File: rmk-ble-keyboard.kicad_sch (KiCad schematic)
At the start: 1 part

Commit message: add matrix
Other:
- added sheet matrix (matrix.kicad_sch)
- title: (none) -> rmk-ble-keyboard
- moved on the sheet: U1
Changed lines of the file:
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@@
 	(generator_version "8.0")
 	(paper "A4")
+	(title_block
+		(title "rmk-ble-keyboard")
+		(date "2024-05-03")
+		(rev "0")
+	)
 	(symbol
 		(lib_id "E73_2G4M08S1C:E73-2G4M08S1C")
-		(at 147.32 88.9 0)
+		(at 60.96 49.53 0)
 		(unit 1)
 		(exclude_from_sim no)
@@
 		(fields_autoplaced yes)
 		(property "Reference" "U1"
-			(at 146.685 59.69 0)
+			(at 60.325 20.32 0)
 			(effects
 				(font
@@
 		)
 		(property "Value" "~"
-			(at 146.685 62.23 0)
+			(at 60.325 22.86 0)
 			(effects
 				(font
@@
 		)
 		(property "Footprint" "E73_2G4M08S1C:E73(2G4M08S1C)"
-			(at 147.32 88.9 0)
+			(at 60.96 49.53 0)
 			(effects
 				(font
@@
 		)
 		(property "Datasheet" ""
-			(at 147.32 88.9 0)
+			(at 60.96 49.53 0)
 			(effects
 				(font
@@
 		)
 		(property "Description" ""
-			(at 147.32 88.9 0)
+			(at 60.96 49.53 0)
 			(effects
 				(font
@@
 				)
 			)
+		)
+	)
+	(sheet
+		(at 246.38 20.32)
+		(size 33.02 138.43)
+		(fields_autoplaced yes)
+		(stroke
+			(width 0.1524)
+			(type solid)
+		)
+		(fill
+			(color 0 0 0 0.0000)
+		)
+		(property "Sheetname" "matrix"
+			(at 246.38 19.6084 0)
+			(effects
+				(font
+					(size 1.27 1.27)
+				)
+				(justify left bottom)
+			)
+		)
+		(property "Sheetfile" "matrix.kicad_sch"
+			(at 246.38 159.3346 0)
+			(effects
+				(font
+					(size 1.27 1.27)
+				)
+				(justify left top)
+			)
+		)
+		(instances
+			(project "rmk-ble-keyboard"
+				(path "/5823a915-d0ed-4262-9b2d-d2247405cf69"
+					(page "2")
+				)
+			)

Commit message: add usb & esd
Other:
- added sheet power (power.kicad_sch)
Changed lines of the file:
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@@
+		)
+	)
+	(sheet
+		(at 189.23 20.32)
+		(size 52.07 34.29)
+		(fields_autoplaced yes)
+		(stroke
+			(width 0.1524)
+			(type solid)
+		)
+		(fill
+			(color 0 0 0 0.0000)
+		)
+		(property "Sheetname" "power"
+			(at 189.23 19.6084 0)
+			(effects
+				(font
+					(size 1.27 1.27)
+				)
+				(justify left bottom)
+			)
+		)
+		(property "Sheetfile" "power.kicad_sch"
+			(at 189.23 55.1946 0)
+			(effects
+				(font
+					(size 1.27 1.27)
+				)
+				(justify left top)
+			)
+		)
+		(instances
+			(project "rmk-ble-keyboard"
+				(path "/5823a915-d0ed-4262-9b2d-d2247405cf69"
+					(page "3")
+				)
+			)
 		)
 	)

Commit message: add power
Signed-off-by: HaoboGu <haobogu@outlook.com>
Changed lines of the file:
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@@
 	)
 	(sheet
-		(at 189.23 20.32)
+		(at 171.45 17.78)
 		(size 52.07 34.29)
 		(fields_autoplaced yes)
@@
 		)
 		(property "Sheetname" "power"
-			(at 189.23 19.6084 0)
+			(at 171.45 17.0684 0)
 			(effects
 				(font
@@
 		)
 		(property "Sheetfile" "power.kicad_sch"
-			(at 189.23 55.1946 0)
+			(at 171.45 52.6546 0)
 			(effects
 				(font

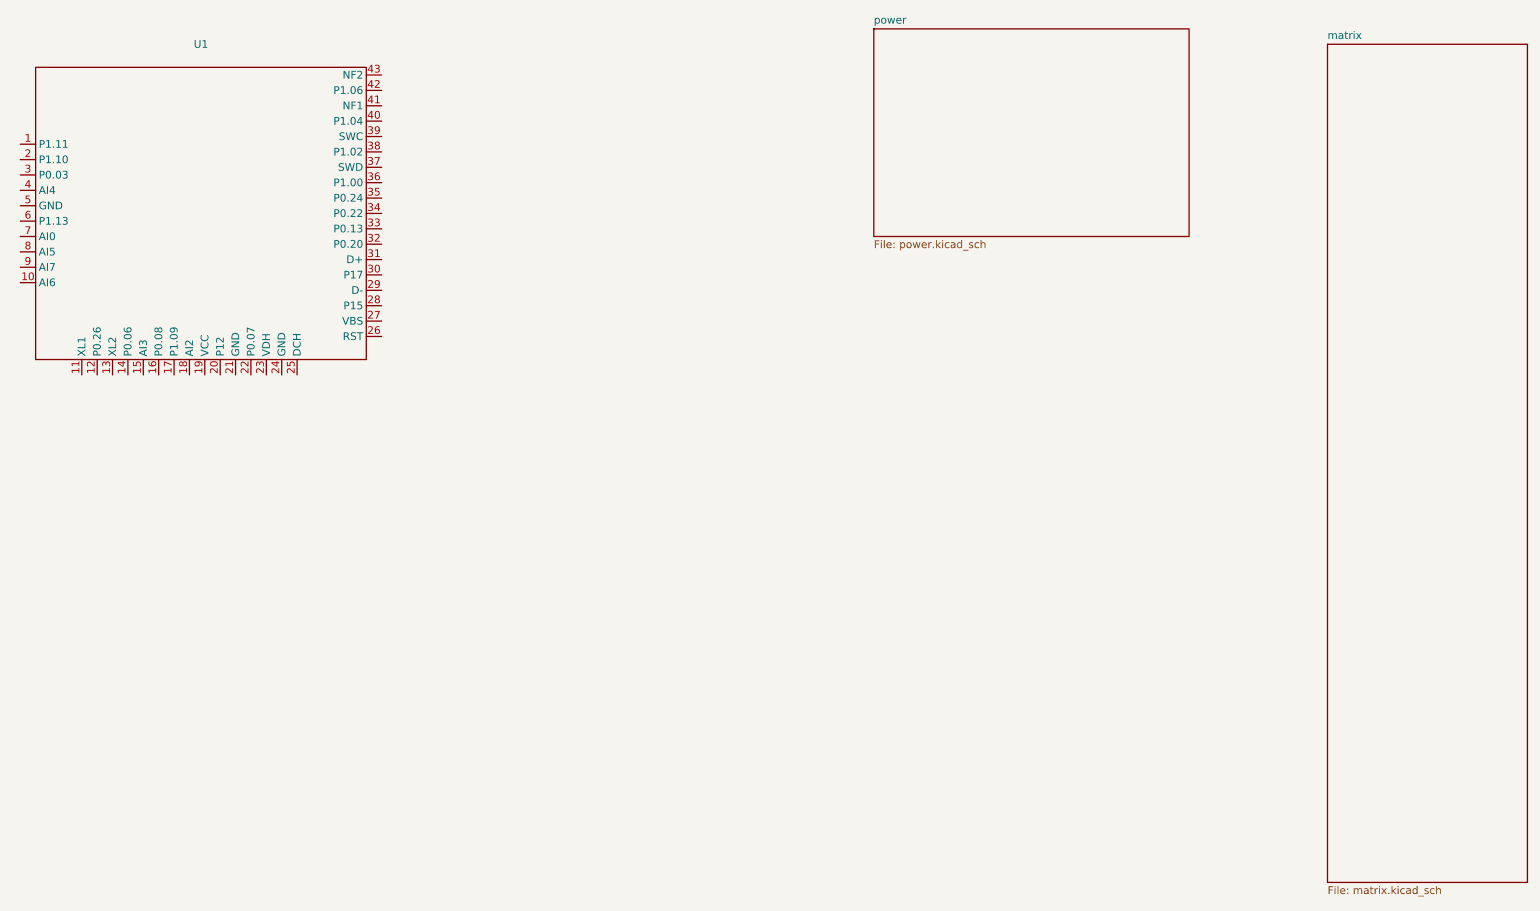
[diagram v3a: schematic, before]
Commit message: add e73 pin out in schema
Signed-off-by: HaoboGu <haobogu@outlook.com>
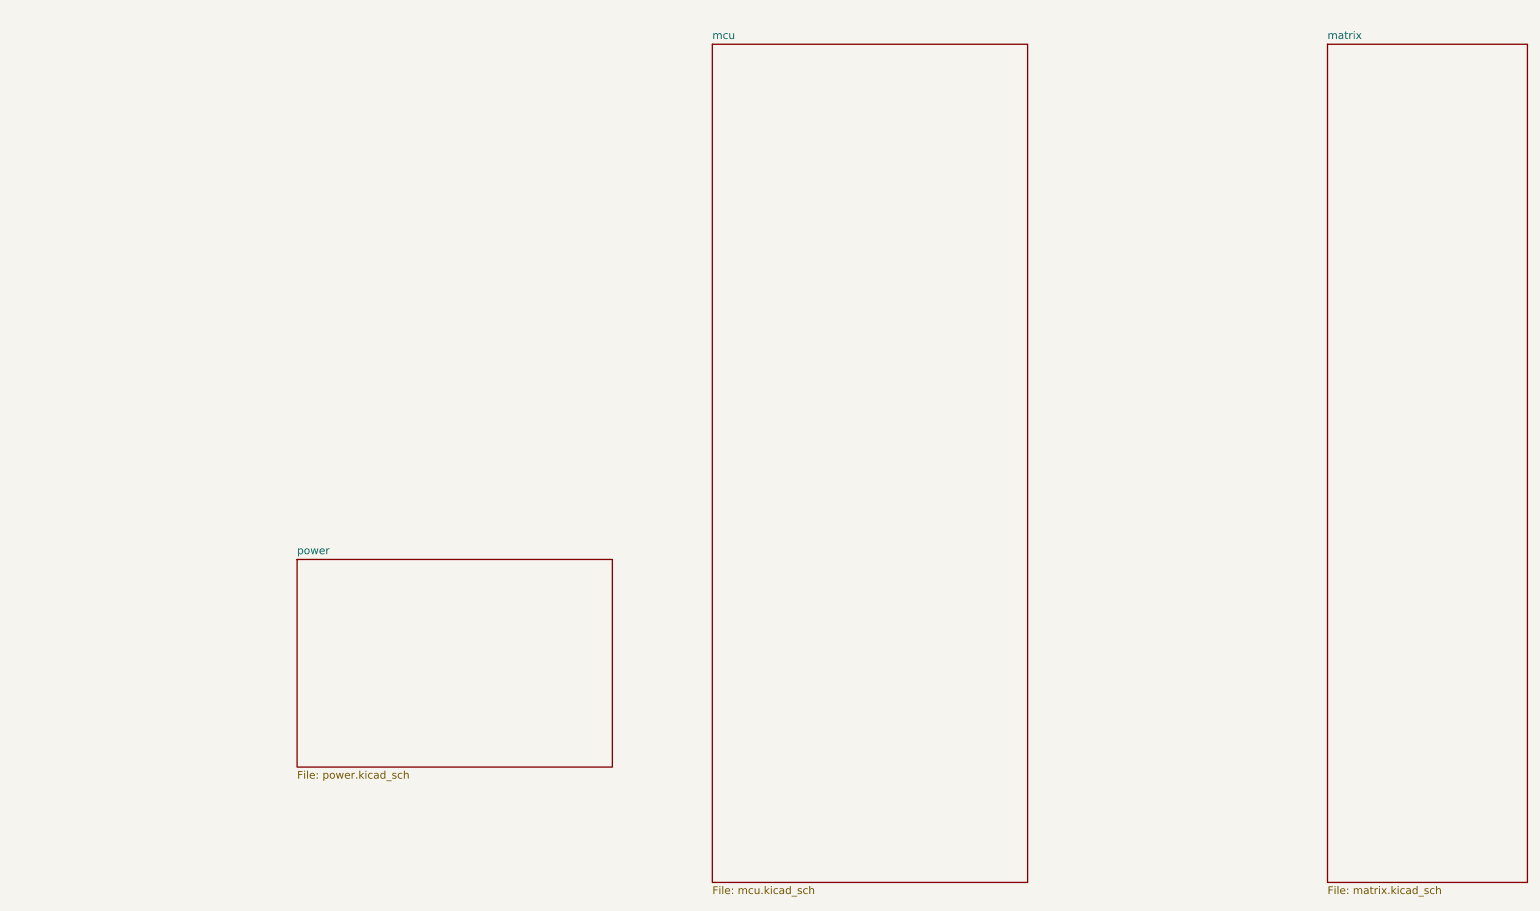
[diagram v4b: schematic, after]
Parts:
- removed U1: ~, E73_2G4M08S1C:E73(2G4M08S1C), symbol E73_2G4M08S1C:E73-2G4M08S1C
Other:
- added sheet mcu (mcu.kicad_sch)
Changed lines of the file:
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@@
 		(rev "0")
 	)
-	(symbol
-		(lib_id "E73_2G4M08S1C:E73-2G4M08S1C")
-		(at 60.96 49.53 0)
-		(unit 1)
-		(exclude_from_sim no)
-		(in_bom yes)
-		(on_board yes)
-		(dnp no)
+	(sheet
+		(at 144.78 20.32)
+		(size 52.07 138.43)
 		(fields_autoplaced yes)
-		(property "Reference" "U1"
-			(at 60.325 20.32 0)
+		(stroke
+			(width 0.1524)
+			(type solid)
+		)
+		(fill
+			(color 0 0 0 0.0000)
+		)
+		(property "Sheetname" "mcu"
+			(at 144.78 19.6084 0)
 			(effects
 				(font
 					(size 1.27 1.27)
 				)
+				(justify left bottom)
 			)
 		)
-		(property "Value" "~"
-			(at 60.325 22.86 0)
+		(property "Sheetfile" "mcu.kicad_sch"
+			(at 144.78 159.3346 0)
 			(effects
 				(font
 					(size 1.27 1.27)
 				)
+				(justify left top)
 			)
-		)
-		(property "Footprint" "E73_2G4M08S1C:E73(2G4M08S1C)"
-			(at 60.96 49.53 0)
-			(effects
-				(font
-					(size 1.27 1.27)
-				)
-				(hide yes)
-			)
-		)
-		(property "Datasheet" ""
-			(at 60.96 49.53 0)
-			(effects
-				(font
-					(size 1.27 1.27)
-				)
-				(hide yes)
-			)
-		)
-		(property "Description" ""
-			(at 60.96 49.53 0)
-			(effects
-				(font
-					(size 1.27 1.27)
-				)
-				(hide yes)
-			)
-		)
-		(pin "27"
-		)
-		(pin "28"
-		)
-		(pin "37"
-		)
-		(pin "20"
-		)
-		(pin "41"
-		)
-		(pin "38"
-		)
-		(pin "29"
-		)
-		(pin "8"
-		)
-		(pin "9"
-		)
-		(pin "43"
-		)
-		(pin "1"
-		)
-		(pin "10"
-		)
-		(pin "11"
-		)
-		(pin "23"
-		)
-		(pin "21"
-		)
-		(pin "22"
-		)
-		(pin "42"
-		)
-		(pin "33"
-		)
-		(pin "30"
-		)
-		(pin "26"
-		)
-		(pin "7"
-		)
-		(pin "39"
-		)
-		(pin "17"
-		)
-		(pin "4"
-		)
-		(pin "2"
-		)
-		(pin "19"
-		)
-		(pin "36"
-		)
-		(pin "34"
-		)
-		(pin "24"
-		)
-		(pin "16"
-		)
-		(pin "35"
-		)
-		(pin "25"
-		)
-		(pin "40"
-		)
-		(pin "12"
-		)
-		(pin "18"
-		)
-		(pin "3"
-		)
-		(pin "32"
-		)
-		(pin "31"
-		)
-		(pin "6"
-		)
-		(pin "13"
-		)
-		(pin "15"
-		)
-		(pin "14"
-		)
-		(pin "5"
 		)
 		(instances
 			(project "rmk-ble-keyboard"
 				(path "/5823a915-d0ed-4262-9b2d-d2247405cf69"
-					(reference "U1")
-					(unit 1)
+					(page "4")
 				)
 			)
@@
 	)
 	(sheet
-		(at 171.45 17.78)
+		(at 76.2 105.41)
 		(size 52.07 34.29)
 		(fields_autoplaced yes)
@@
 		)
 		(property "Sheetname" "power"
-			(at 171.45 17.0684 0)
+			(at 76.2 104.6984 0)
 			(effects
 				(font
@@
 		)
 		(property "Sheetfile" "power.kicad_sch"
-			(at 171.45 52.6546 0)
+			(at 76.2 140.2846 0)
 			(effects
 				(font

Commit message: schema: rev0 done
Signed-off-by: HaoboGu <haobogu@outlook.com>
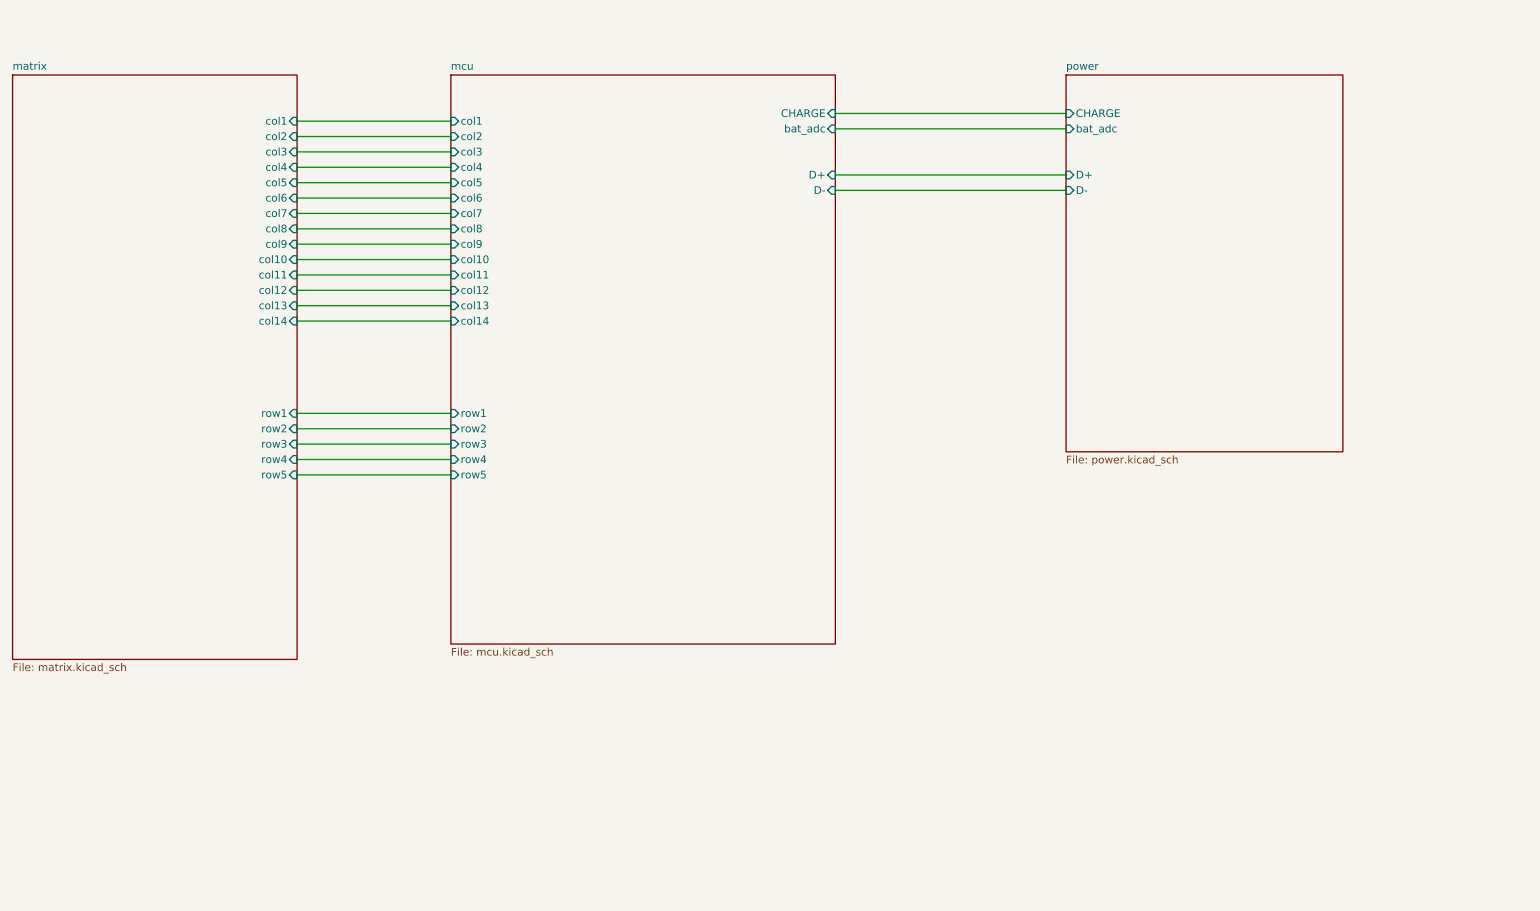
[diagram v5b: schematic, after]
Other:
- sheet matrix ports: added col1, col10, col11, col12, col13, col14, col2, col3, col4, col5, col6, col7, col8, col9, row1, row2, row3, row4, row5; removed none
- sheet mcu ports: added CHARGE, D+, D-, bat_adc, col1, col10, col11, col12, col13, col14, col2, col3, col4, col5, col6, col7, col8, col9, row1, row2, row3, row4, row5; removed none
- sheet power ports: added CHARGE, D+, D-, bat_adc; removed none
